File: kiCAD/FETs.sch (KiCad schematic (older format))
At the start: 0 parts

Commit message: Completed Schematic, assigned footprints.
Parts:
- added C136, C137: 100n, Capacitor_SMD:C_0603_1608Metric_Pad1.05x0.95mm_HandSolder, symbol Device:C_Small
- added C138, C139, C140, C141, C142, C143, C144, C145, C146, C147: 10u, Capacitor_SMD:C_1206_3216Metric_Pad1.42x1.75mm_HandSolder, symbol Device:C_Small
- added D13, D18, D25, D32: LED_Small, Diode_SMD:D_0603_1608Metric_Pad1.05x0.95mm_HandSolder, symbol Device:LED_Small
- added D14, D15, D19, D20, D21, D26, D28, D29, D33, D35: SK310A-TP, Diode_SMD:D_SMA_Handsoldering, symbol Device:D_Schottky
- added D16, D17, D22, D23, D24, D27, D30, D31, D34, D36: RSB39VTE-17, Diode_SMD:D_SOD-323F, symbol Device:D_TVS
- added F6, F7, F8: 3.5A, Fuse:Fuseholder_Littelfuse_Nano2_157x, symbol Device:Fuse
- added J12: H0, Connector_Molex:Molex_KK-396_A-41791-0002_1x02_P3.96mm_Vertical, symbol Connector_Generic:Conn_01x02
- added J13: F0, Connector_Molex:Molex_KK-254_AE-6410-02A_1x02_P2.54mm_Vertical, symbol Connector_Generic:Conn_01x02
- added J14, J18: V_SELECT, Connector_PinHeader_2.54mm:PinHeader_2x03_P2.54mm_Vertical, symbol Connector_Generic:Conn_02x03_Odd_Even
- added J15: F1, Connector_Molex:Molex_KK-254_AE-6410-02A_1x02_P2.54mm_Vertical, symbol Connector_Generic:Conn_01x02
- added J16: F4, Connector_Molex:Molex_KK-254_AE-6410-02A_1x02_P2.54mm_Vertical, symbol Connector_Generic:Conn_01x02
- added J17: H1, Connector_Molex:Molex_KK-396_A-41791-0002_1x02_P3.96mm_Vertical, symbol Connector_Generic:Conn_01x02
- added J19: F2, Connector_Molex:Molex_KK-254_AE-6410-02A_1x02_P2.54mm_Vertical, symbol Connector_Generic:Conn_01x02
- added J20: F5, Connector_Molex:Molex_KK-254_AE-6410-02A_1x02_P2.54mm_Vertical, symbol Connector_Generic:Conn_01x02
- added J21: H2, Connector_Molex:Molex_KK-396_A-41791-0002_1x02_P3.96mm_Vertical, symbol Connector_Generic:Conn_01x02
- added J22: F3, Connector_Molex:Molex_KK-254_AE-6410-02A_1x02_P2.54mm_Vertical, symbol Connector_Generic:Conn_01x02
- added J23: HB, TerminalBlock_Dinkle:TerminalBlock_Dinkle_DT-55-B01X-02_P10.00mm, symbol Connector_Generic:Conn_01x02
- added JP3, JP4, JP5, JP6: Jumper_3_Open, Connector_PinHeader_2.54mm:PinHeader_1x03_P2.54mm_Vertical, symbol Jumper:Jumper_3_Open
- added Q1, Q3, Q4, Q6, Q7, Q9: Q_NMOS_GSD, Package_TO_SOT_SMD:SOT-23_Handsoldering, symbol Device:Q_NMOS_GSD
- added Q10, Q2, Q5, Q8: Q_NMOS_GDS, Package_TO_SOT_SMD:TO-252-2, symbol Device:Q_NMOS_GDS
- added R44, R45, R46, R47, R48, R49, R50, R51, R52, R53: 10k, Resistor_SMD:R_0603_1608Metric_Pad1.05x0.95mm_HandSolder, symbol Device:R_Small_US
- added R54, R55, R57, R58, R59, R61, R62, R63, R65, R66: 100, Resistor_SMD:R_0603_1608Metric_Pad1.05x0.95mm_HandSolder, symbol Device:R_Small_US
- added R56, R60, R64, R67: 2.2k, Resistor_SMD:R_0603_1608Metric_Pad1.05x0.95mm_HandSolder, symbol Device:R_Small_US
- added U13, U14: 74HCT365, Package_SO:SSOP-16_5.3x6.2mm_P0.65mm, symbol MOSFET_Drivers:74HCT365
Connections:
- new net: Q2.1 (G), R55.1
- new net: C138.1, D13.1 (K), D14.2 (A), D17.1 (A1), J12.2 (Pin_2), Q2.2 (D)
- new net: Q1.1 (G), R54.1
- new net: C139.1, D15.2 (A), D16.1 (A1), J13.2 (Pin_2), Q1.3 (D)
- new net: D13.2 (A), R56.2
- new net: F6.2, J12.1 (Pin_1)
- new net: Q5.1 (G), R59.1
- new net: C142.1, D18.1 (K), D21.2 (A), D24.1 (A1), J17.2 (Pin_2), Q5.2 (D)
- new net: D18.2 (A), R60.2
- new net: F7.2, J17.1 (Pin_1)
- new net: Q8.1 (G), R63.1
- new net: C144.1, D25.1 (K), D28.2 (A), D31.1 (A1), J21.2 (Pin_2), Q8.2 (D)
- new net: D25.2 (A), R64.2
- new net: F8.2, J21.1 (Pin_1)
- new net: Q10.1 (G), R66.1
- new net: C147.1, D32.1 (K), D35.2 (A), D36.1 (A1), J23.2 (Pin_2), Q10.2 (D)
- new net: D32.2 (A), R67.2
- new net: C139.2, D15.1 (K), J13.1 (Pin_1), JP3.2 (C)
- new net: Q3.1 (G), R57.1
- new net: C140.1, D19.2 (A), D22.1 (A1), J15.2 (Pin_2), Q3.3 (D)
- new net: C140.2, D19.1 (K), J15.1 (Pin_1), JP4.2 (C)
- new net: Q6.1 (G), R61.1
- new net: C143.1, D26.2 (A), D27.1 (A1), J19.2 (Pin_2), Q6.3 (D)
- new net: C143.2, D26.1 (K), J19.1 (Pin_1), JP5.2 (C)
- new net: Q9.1 (G), R65.1
- new net: C146.1, D33.2 (A), D34.1 (A1), J22.2 (Pin_2), Q9.3 (D)
- new net: C146.2, D33.1 (K), J22.1 (Pin_1), JP6.2 (C)
- new net: Q4.1 (G), R58.1
- new net: C141.1, D20.2 (A), D23.1 (A1), J16.2 (Pin_2), Q4.3 (D)
- new net: C141.2, D20.1 (K), J14.2 (Pin_2), J14.4 (Pin_4), J14.6 (Pin_6), J16.1 (Pin_1)
- new net: Q7.1 (G), R62.1
- new net: C145.1, D29.2 (A), D30.1 (A1), J20.2 (Pin_2), Q7.3 (D)
- new net: C145.2, D29.1 (K), J18.2 (Pin_2), J18.4 (Pin_4), J18.6 (Pin_6), J20.1 (Pin_1)
- new net +12V: J14.3 (Pin_3), J18.3 (Pin_3), JP3.1 (A), JP4.1 (A), JP5.1 (A), JP6.1 (A)
- new net +24V: C138.2, C142.2, C144.2, D14.1 (K), D21.1 (K), D28.1 (K), F6.1, F7.1, F8.1, J14.1 (Pin_1), J18.1 (Pin_1), JP3.3 (B), JP4.3 (B), JP5.3 (B), JP6.3 (B), R56.1, R60.1, R64.1
- new net +5V: C136.2, C137.2, J14.5 (Pin_5), J18.5 (Pin_5), U13.16 (VCC), U14.16 (VCC)
- new net BED_HEATER: R52.1, U14.12 (5A), U14.14 (6A)
- new net BED_HEATER_BUFF: R66.2, U14.11 (5Y), U14.13 (6Y)
- new net FAN0: R44.1, U13.2 (1A)
- new net FAN0_BUFF: R54.2, U13.3 (1Y)
- new net FAN1: R45.1, U13.4 (2A)
- new net FAN1_BUFF: R57.2, U13.5 (2Y)
- new net FAN2: R47.1, U13.6 (3A)
- new net FAN2_BUFF: R61.2, U13.7 (3Y)
- new net FAN3: R49.1, U13.10 (4A)
- new net FAN3_BUFF: R65.2, U13.9 (4Y)
- new net FAN4: R51.1, U13.12 (5A)
- new net FAN4_BUFF: R58.2, U13.11 (5Y)
- new net FAN5: R53.1, U13.14 (6A)
- new net FAN5_BUFF: R62.2, U13.13 (6Y)
- new net GND: C136.1, C137.1, D16.2 (A2), D17.2 (A2), D22.2 (A2), D23.2 (A2), D24.2 (A2), D27.2 (A2), D30.2 (A2), D31.2 (A2), D34.2 (A2), D36.2 (A2), Q1.2 (S), Q10.3 (S), Q2.3 (S), Q3.2 (S), Q4.2 (S), Q5.3 (S), Q6.2 (S), Q7.2 (S), Q8.3 (S), Q9.2 (S), R44.2, R45.2, R46.2, R47.2, R48.2, R49.2, R50.2, R51.2, R52.2, R53.2, U13.1 (~OE1), U13.15 (~OE2), U13.8 (GND), U14.1 (~OE1), U14.15 (~OE2), U14.8 (GND)
- new net HEATER0: R46.1, U14.2 (1A)
- new net HEATER0_BUFF: R55.2, U14.3 (1Y)
- new net HEATER1: R48.1, U14.4 (2A)
- new net HEATER1_BUFF: R59.2, U14.5 (2Y)
- new net HEATER2: R50.1, U14.10 (4A), U14.6 (3A)
- new net HEATER2_BUFF: R63.2, U14.7 (3Y), U14.9 (4Y)
- new net VBED: C147.2, D35.1 (K), J23.1 (Pin_1), R67.1
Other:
- note added: "BED MOSFET - IPD036N04L"
- note added: "DRIVERS\n"
- note added: "FAN MOSFET - CSD18532\n"
- note added: "FANS\n"
- note added: "HEATERS\n"
- note added: "HOTEND MOSFET - AOD4184A"
- note added: "LITTELFUSE NANO2 FUSE HOLDER"
- note added: "MOLEX KK-254"
- note added: "MOLEX KK-396\n"
- note added: "SSOP-16 Package"

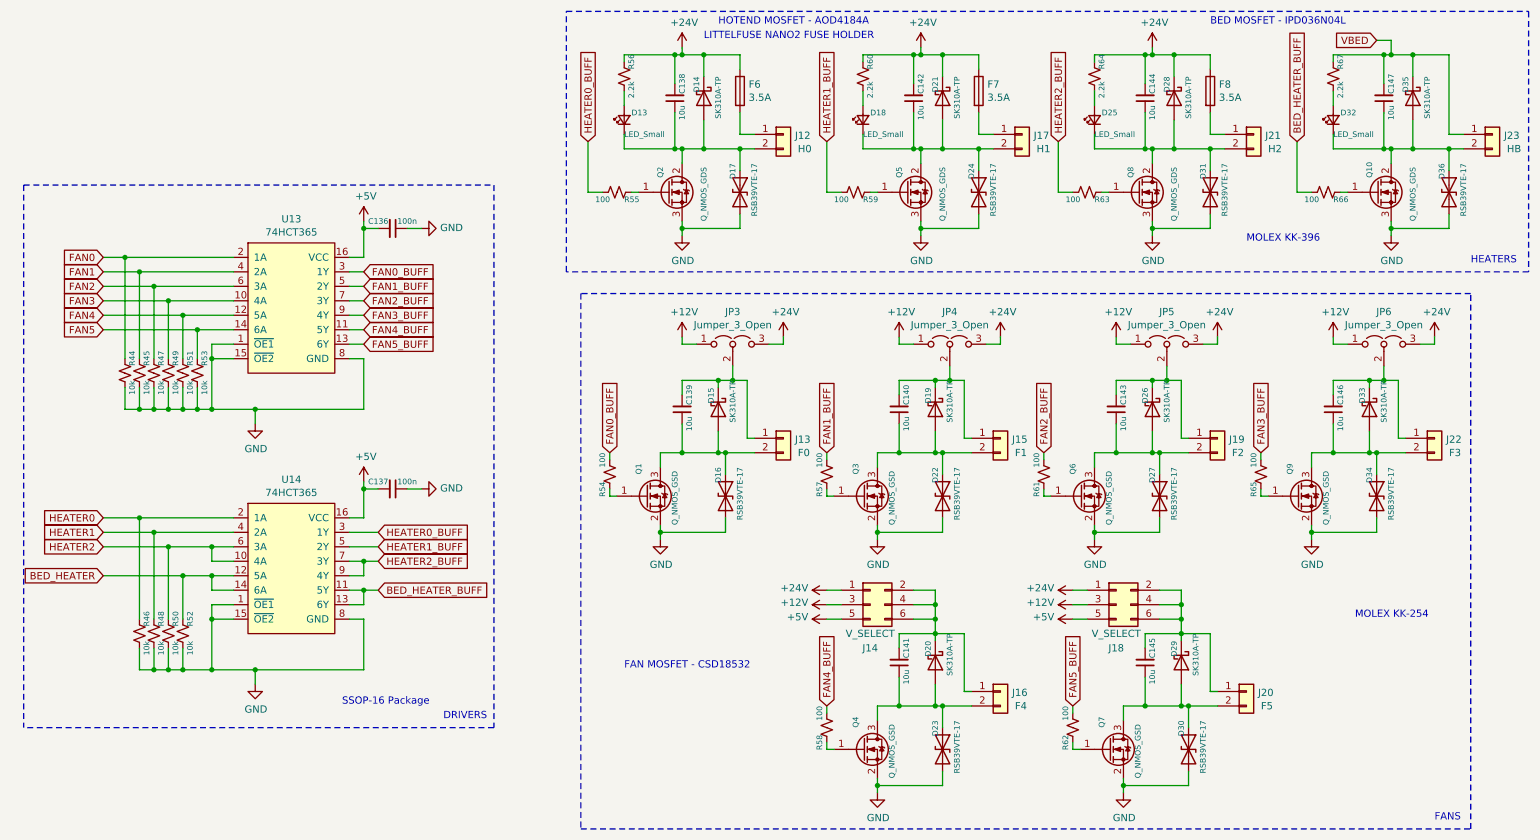
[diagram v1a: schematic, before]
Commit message: did layout for FETs and redid layout for Power input
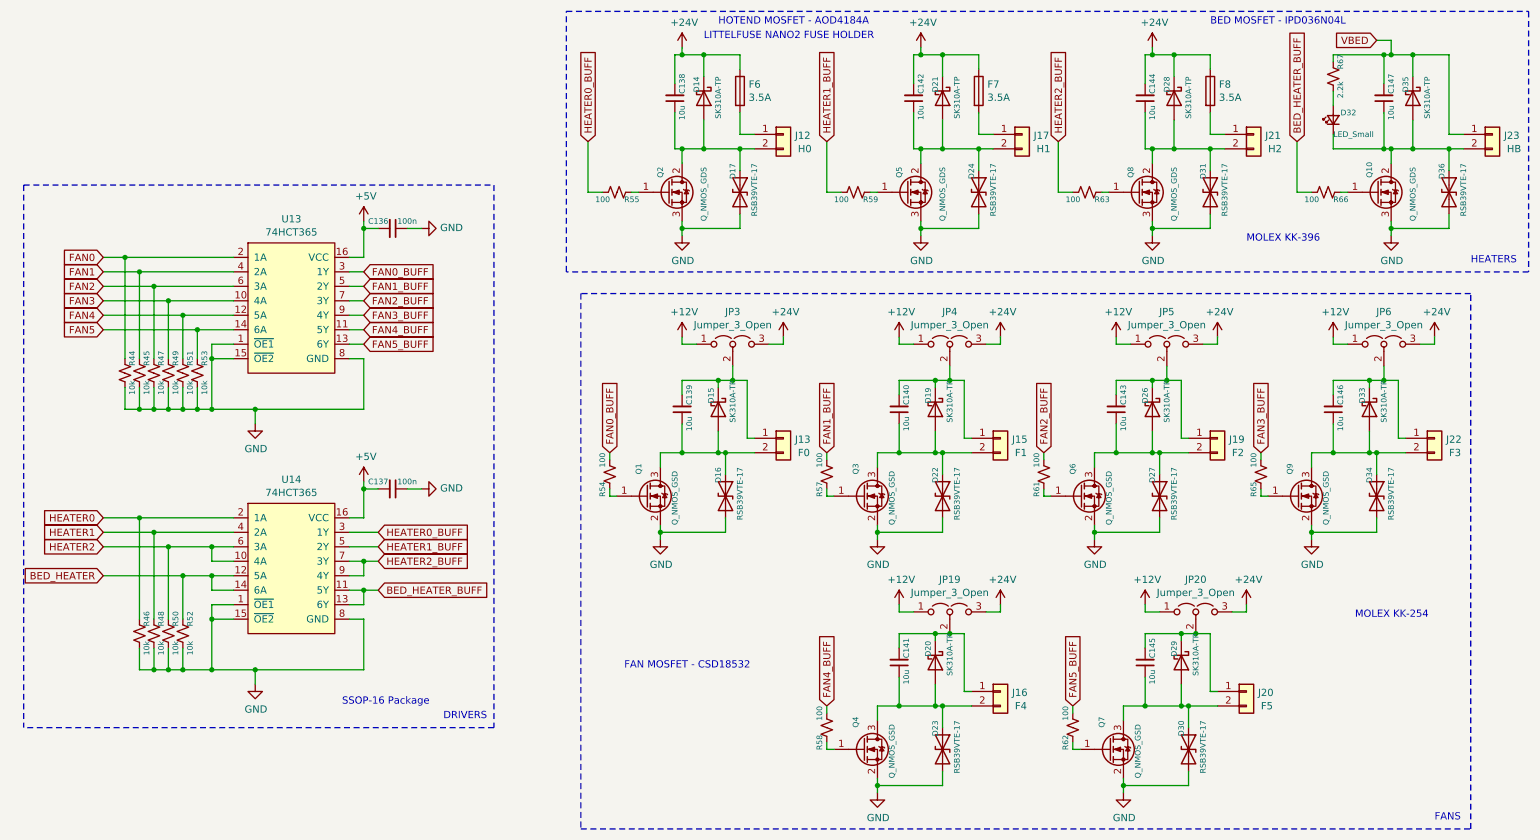
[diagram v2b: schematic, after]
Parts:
- removed D13, D18, D25: LED_Small, Diode_SMD:D_0603_1608Metric_Pad1.05x0.95mm_HandSolder, symbol Device:LED_Small
- removed J14, J18: V_SELECT, Connector_PinHeader_2.54mm:PinHeader_2x03_P2.54mm_Vertical, symbol Connector_Generic:Conn_02x03_Odd_Even
- removed R56, R60, R64: 2.2k, Resistor_SMD:R_0603_1608Metric_Pad1.05x0.95mm_HandSolder, symbol Device:R_Small_US
- added JP19, JP20: Jumper_3_Open, Connector_PinHeader_2.54mm:PinHeader_1x03_P2.54mm_Vertical, symbol Jumper:Jumper_3_Open
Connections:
- net +12V: now also JP19.1 (A), JP20.1 (A)
- net +24V: now also JP19.3 (B), JP20.3 (B)
- net at C141.2, D20.1 (K), J16.1 (Pin_1): now also JP19.2 (C)
- net at C145.2, D29.1 (K), J20.1 (Pin_1): now also JP20.2 (C)
